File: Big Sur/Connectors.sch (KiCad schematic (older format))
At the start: 2 parts, among them J1 XT90, J2 XT90

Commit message: Work on pump drivers.
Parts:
- added J?: SMD CASTELLATION PKG, symbol Connector_Generic:Conn_02x21_Counter_Clockwise
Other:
- note added: "DON’T REALLY KNOW WHAT WE’RE DOING FOR CONNECTORS.\nSOMETHING ABOUT XT30/60/90S FOR POWER?"
- note added: "Strideduino"
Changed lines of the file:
@@
 Text Notes 1700 1600 0    118  ~ 0
 Power Input
+Text Notes 2950 2550 0    50   ~ 0
+DON’T REALLY KNOW WHAT WE’RE DOING FOR CONNECTORS.\nSOMETHING ABOUT XT30/60/90S FOR POWER?
+$Comp
+L Connector_Generic:Conn_02x21_Counter_Clockwise J?
+U 1 1 5D85E3A4
+P 2150 5350
+F 0 "J?" H 2200 6567 50  0000 C CNN
+F 1 "SMD CASTELLATION PKG" H 2200 6476 50  0000 C CNN
+F 2 "" H 2150 5350 50  0001 C CNN
+F 3 "~" H 2150 5350 50  0001 C CNN
+	1    2150 5350
+	1    0    0    -1
+$EndComp
+Text Notes 1700 4000 0    118  ~ 0
+Strideduino
 $EndSCHEMATC

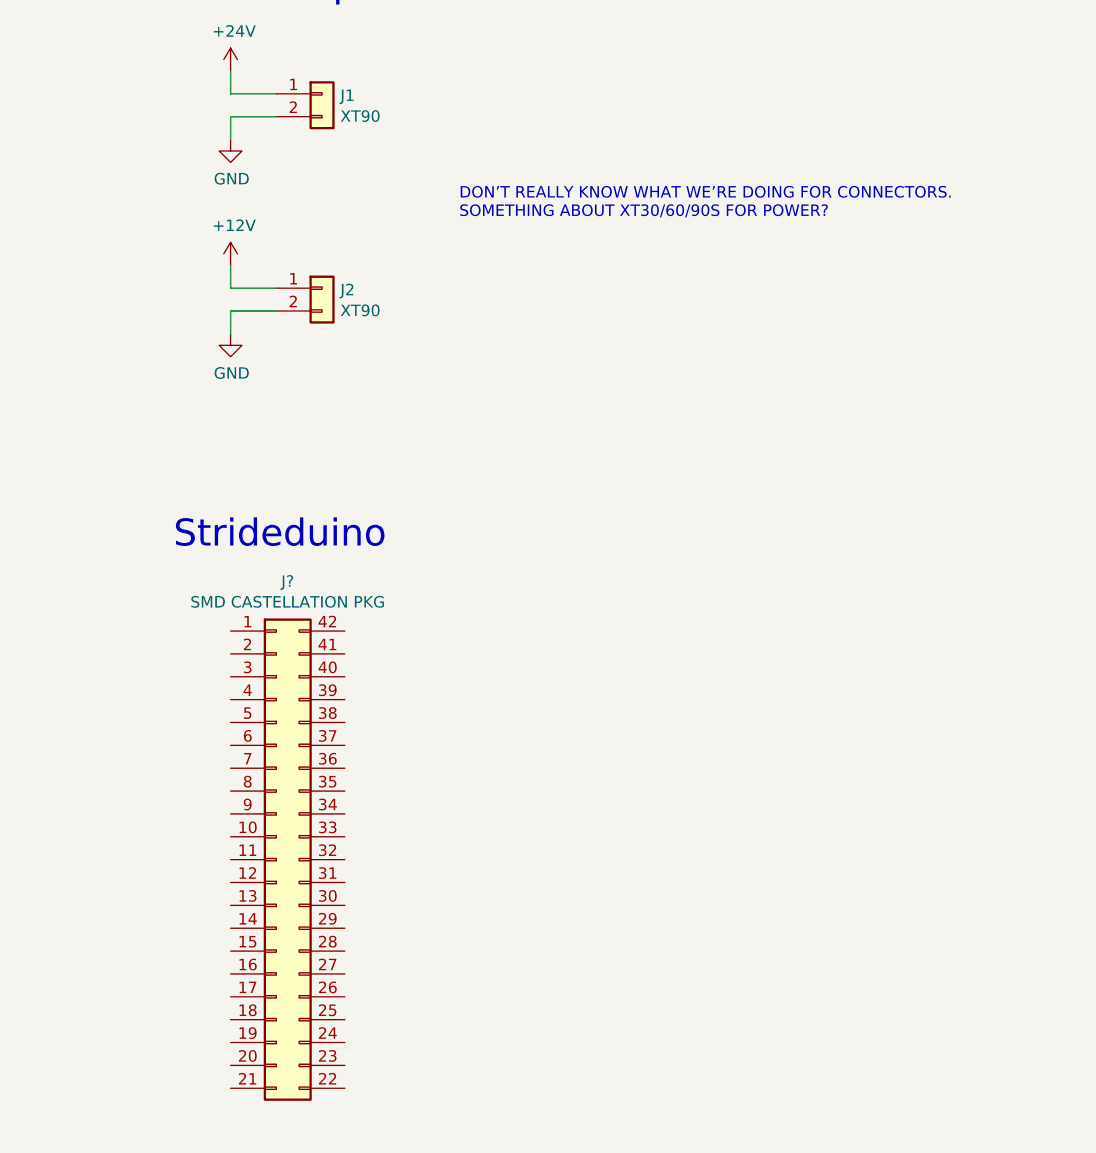
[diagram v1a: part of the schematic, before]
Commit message: Started filling in pinout of Paraduino connector, based on current Paraduino schematic.
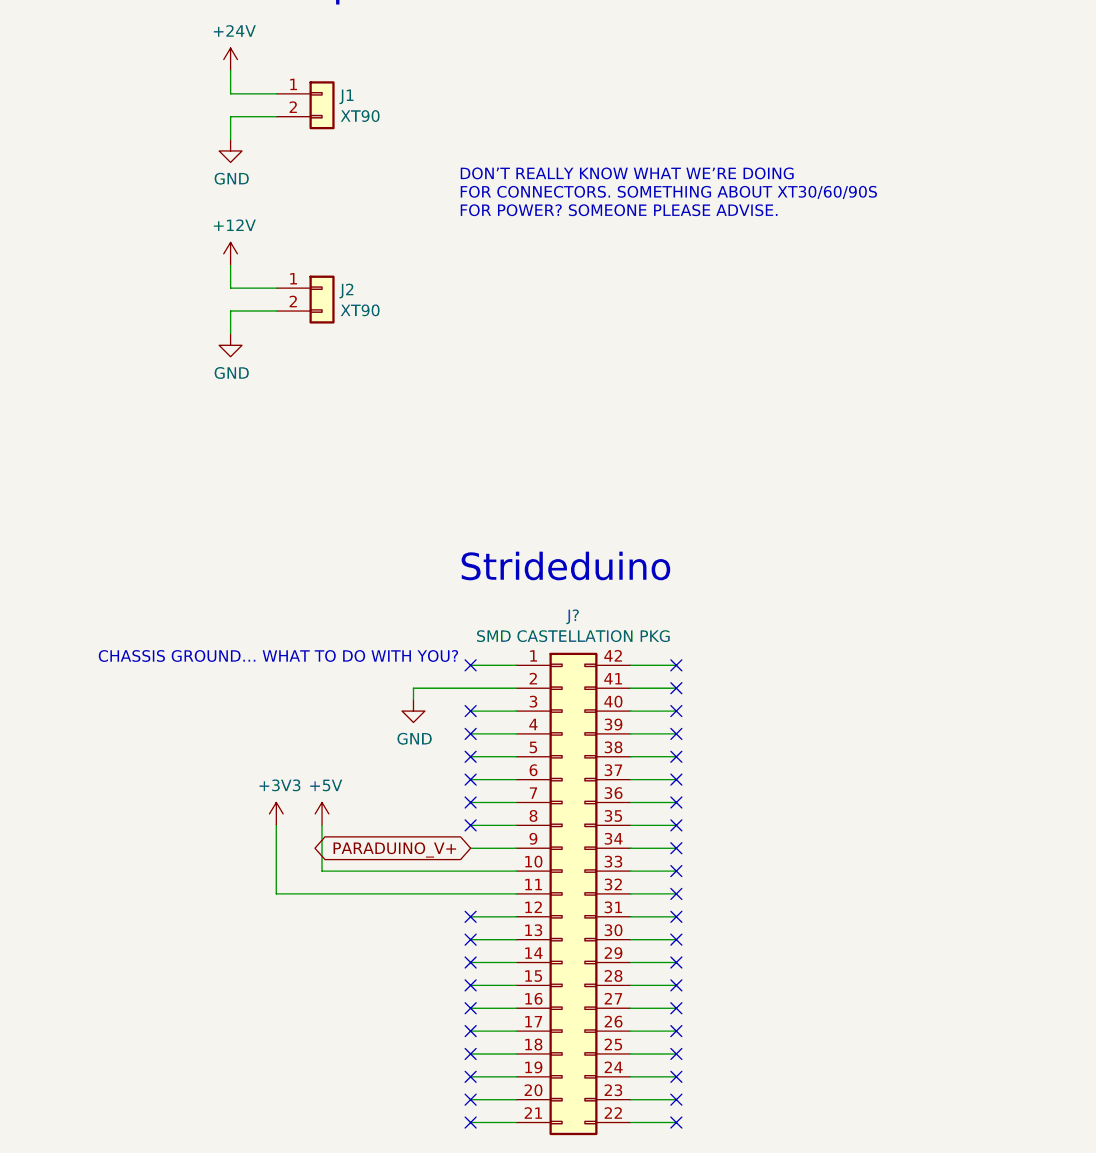
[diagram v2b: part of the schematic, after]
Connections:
- net GND: now also J?.2 (Pin_2)
- net +5V: now reaches J?.10 (Pin_10)
- net +3V3: now reaches J?.11 (Pin_11)
- net PARADUINO_V+: now reaches J?.9 (Pin_9)
- no-connect marks 0 -> 38
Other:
- note added: "CHASSIS GROUND… WHAT TO DO WITH YOU?"
- note added: "DON’T REALLY KNOW WHAT WE’RE DOING\nFOR CONNECTORS. SOMETHING ABOUT XT30/60/90S\nFOR POWER? SOMEONE PLEASE ADVISE."
- note removed: "DON’T REALLY KNOW WHAT WE’RE DOING FOR CONNECTORS.\nSOMETHING ABOUT XT30/60/90S FOR POWER?"
- moved on the sheet: J?
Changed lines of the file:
@@
 Power Input
 Text Notes 2950 2550 0    50   ~ 0
-DON’T REALLY KNOW WHAT WE’RE DOING FOR CONNECTORS.\nSOMETHING ABOUT XT30/60/90S FOR POWER?
+DON’T REALLY KNOW WHAT WE’RE DOING\nFOR CONNECTORS. SOMETHING ABOUT XT30/60/90S\nFOR POWER? SOMEONE PLEASE ADVISE.
 $Comp
 L Connector_Generic:Conn_02x21_Counter_Clockwise J?
 U 1 1 5D85E3A4
-P 2150 5350
-F 0 "J?" H 2200 6567 50  0000 C CNN
-F 1 "SMD CASTELLATION PKG" H 2200 6476 50  0000 C CNN
-F 2 "" H 2150 5350 50  0001 C CNN
-F 3 "~" H 2150 5350 50  0001 C CNN
-	1    2150 5350
+P 3400 5500
+F 0 "J?" H 3450 6717 50  0000 C CNN
+F 1 "SMD CASTELLATION PKG" H 3450 6626 50  0000 C CNN
+F 2 "" H 3400 5500 50  0001 C CNN
+F 3 "~" H 3400 5500 50  0001 C CNN
+	1    3400 5500
 	1    0    0    -1
 $EndComp
-Text Notes 1700 4000 0    118  ~ 0
+Text Notes 2950 4150 0    118  ~ 0
 Strideduino
+Wire Wire Line
+	3000 4500 3200 4500
+NoConn ~ 3000 4500
+Text Notes 2950 4500 2    50   ~ 0
+CHASSIS GROUND… WHAT TO DO WITH YOU?
+Wire Wire Line
+	3200 4600 2750 4600
+Wire Wire Line
+	2750 4600 2750 4650
+$Comp
+L power:GND #PWR?
+U 1 1 5D896FCF
+P 2750 4650
+F 0 "#PWR?" H 2750 4400 50  0001 C CNN
+F 1 "GND" H 2755 4477 50  0000 C CNN
+F 2 "" H 2750 4650 50  0001 C CNN
+F 3 "" H 2750 4650 50  0001 C CNN
+	1    2750 4650
+	1    0    0    -1
+$EndComp
+Wire Wire Line
+	3200 4700 3000 4700
+Wire Wire Line
+	3200 4800 3000 4800
+Wire Wire Line
+	3200 4900 3000 4900
+Wire Wire Line
+	3200 5000 3000 5000
+Wire Wire Line
+	3200 5100 3000 5100
+Wire Wire Line
+	3200 5200 3000 5200
+Wire Wire Line
+	3200 5600 3000 5600
+Wire Wire Line
+	3200 5700 3000 5700
+Wire Wire Line
+	3200 5800 3000 5800
+Wire Wire Line
+	3200 5900 3000 5900
+Wire Wire Line
+	3200 6000 3000 6000
+Wire Wire Line
+	3200 6100 3000 6100
+Wire Wire Line
+	3200 6200 3000 6200
+Wire Wire Line
+	3200 6300 3000 6300
+Wire Wire Line
+	3200 6400 3000 6400
+Wire Wire Line
+	3200 6500 3000 6500
+Wire Wire Line
+	3900 4700 3700 4700
+Wire Wire Line
+	3900 4800 3700 4800
+Wire Wire Line
+	3900 4900 3700 4900
+Wire Wire Line
+	3900 5000 3700 5000
+Wire Wire Line
+	3900 5100 3700 5100
+Wire Wire Line
+	3900 5200 3700 5200
+Wire Wire Line
+	3900 5300 3700 5300
+Wire Wire Line
+	3900 5400 3700 5400
+Wire Wire Line
+	3900 5500 3700 5500
+Wire Wire Line
+	3900 5600 3700 5600
+Wire Wire Line
+	3900 5700 3700 5700
+Wire Wire Line
+	3900 5800 3700 5800
+Wire Wire Line
+	3900 5900 3700 5900
+Wire Wire Line
+	3900 6000 3700 6000
+Wire Wire Line
+	3900 6100 3700 6100
+Wire Wire Line
+	3900 6200 3700 6200
+Wire Wire Line
+	3900 6300 3700 6300
+Wire Wire Line
+	3900 6400 3700 6400
+Wire Wire Line
+	3900 6500 3700 6500
+Wire Wire Line
+	3900 4500 3700 4500
+Wire Wire Line
+	3900 4600 3700 4600
+NoConn ~ 3900 4500
+NoConn ~ 3900 4600
+NoConn ~ 3900 4700
+NoConn ~ 3900 4800
+NoConn ~ 3900 4900
+NoConn ~ 3900 5000
+NoConn ~ 3900 5100
+NoConn ~ 3900 5200
+NoConn ~ 3900 5300
+NoConn ~ 3900 5400
+NoConn ~ 3900 5500
+NoConn ~ 3900 5600
+NoConn ~ 3900 5700
+NoConn ~ 3900 5800
+NoConn ~ 3900 5900
+NoConn ~ 3900 6000
+NoConn ~ 3900 6100
+NoConn ~ 3900 6200
+NoConn ~ 3900 6300
+NoConn ~ 3900 6400
+NoConn ~ 3900 6500
+NoConn ~ 3000 6500
+NoConn ~ 3000 6400
+NoConn ~ 3000 6300
+NoConn ~ 3000 6200
+NoConn ~ 3000 6100
+NoConn ~ 3000 6000
+NoConn ~ 3000 5900
+NoConn ~ 3000 5800
+NoConn ~ 3000 5700
+NoConn ~ 3000 5600
+NoConn ~ 3000 5200
+NoConn ~ 3000 5100
+NoConn ~ 3000 5000
+NoConn ~ 3000 4900
+NoConn ~ 3000 4800
+NoConn ~ 3000 4700
+$Comp
+L power:+5V #PWR?
+U 1 1 5D8BF1CA
+P 2350 5200
+F 0 "#PWR?" H 2350 5050 50  0001 C CNN
+F 1 "+5V" H 2365 5373 50  0000 C CNN
+F 2 "" H 2350 5200 50  0001 C CNN
+F 3 "" H 2350 5200 50  0001 C CNN
+	1    2350 5200
+	1    0    0    -1
+$EndComp
+Wire Wire Line
+	2350 5200 2350 5400
+Wire Wire Line
+	2350 5400 3200 5400
+$Comp
+L power:+3V3 #PWR?
+U 1 1 5D8C1FAE
+P 2150 5200
+F 0 "#PWR?" H 2150 5050 50  0001 C CNN
+F 1 "+3V3" H 2165 5373 50  0000 C CNN
+F 2 "" H 2150 5200 50  0001 C CNN
+F 3 "" H 2150 5200 50  0001 C CNN
+	1    2150 5200
+	1    0    0    -1
+$EndComp
+Wire Wire Line
+	2150 5200 2150 5500
+Wire Wire Line
+	2150 5500 3200 5500
+Wire Wire Line
+	3000 5300 3200 5300
+Text GLabel 3000 5300 0    50   BiDi ~ 0
+PARADUINO_V+
 $EndSCHEMATC

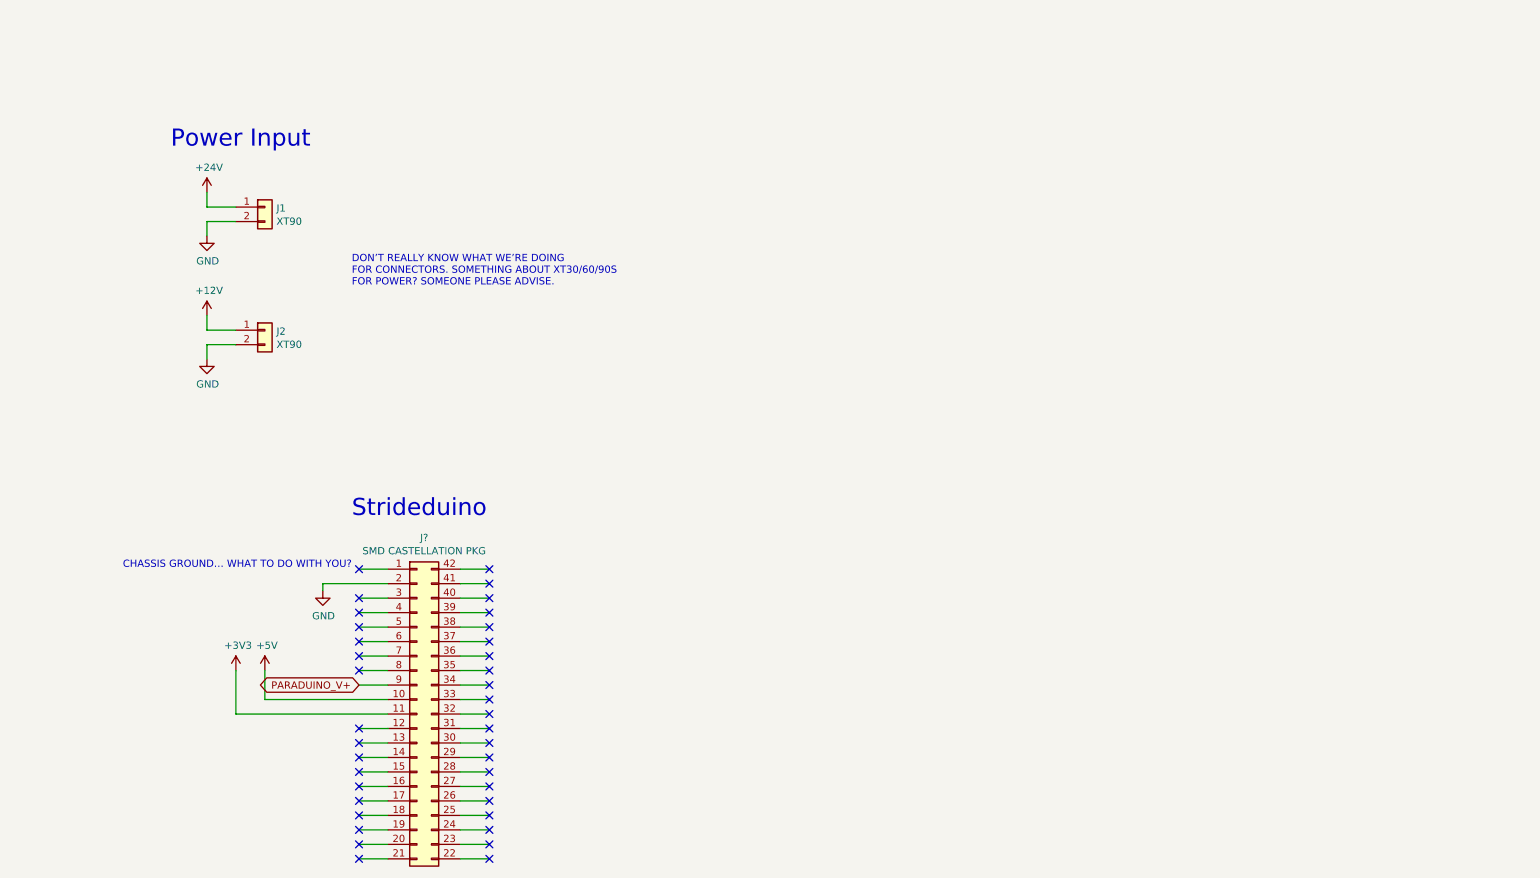
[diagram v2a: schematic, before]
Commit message: Updated current sense, second pump driver, solenoid connectors
-Current sense now uses current sense ICs, connected to Paraduino ADC pins.
-Added second pump driver.
-Connected outputs with XT30 connectors.
-Still need some Paraduino connections, inverter driver, footprints.
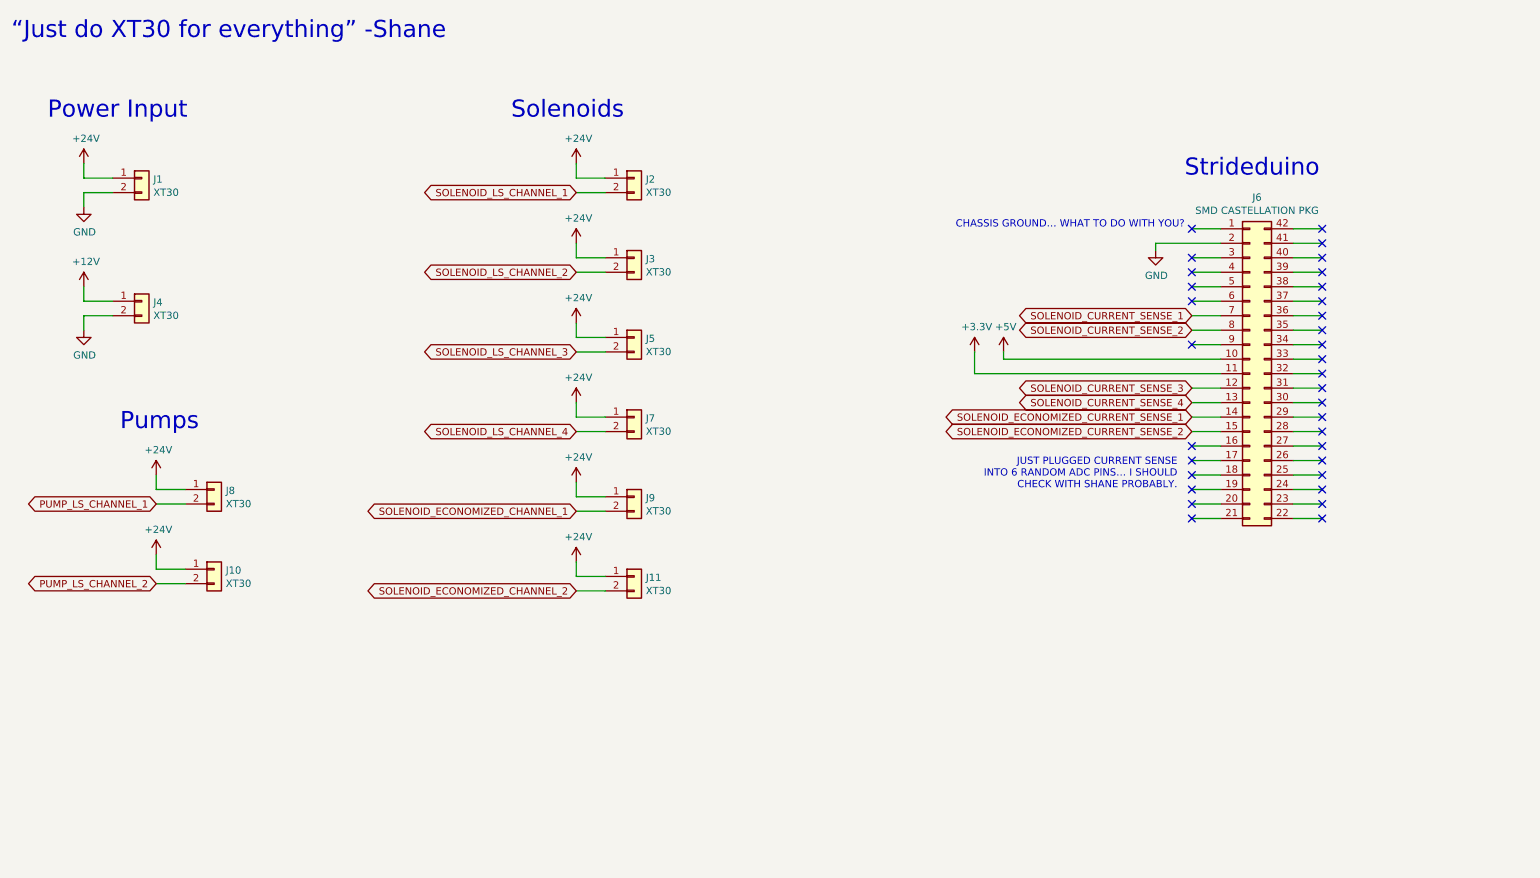
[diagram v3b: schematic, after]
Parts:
- added J10, J11, J2, J3, J5, J7, J8, J9: XT30, symbol Connector_Generic:Conn_01x02
- J1: value XT90 -> XT30
- J4: renamed from J2; value XT90 -> XT30
- gave numbers to parts that had none: 1
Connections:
- net +24V: now also J10.1 (Pin_1), J11.1 (Pin_1), J2.1 (Pin_1), J3.1 (Pin_1), J5.1 (Pin_1), J7.1 (Pin_1), J8.1 (Pin_1), J9.1 (Pin_1)
- net SOLENOID_CURRENT_SENSE_3: now reaches J6.12 (Pin_12)
- net SOLENOID_CURRENT_SENSE_4: now reaches J6.13 (Pin_13)
- net SOLENOID_ECONOMIZED_CURRENT_SENSE_1: now reaches J6.14 (Pin_14)
- net SOLENOID_ECONOMIZED_CURRENT_SENSE_2: now reaches J6.15 (Pin_15)
- net SOLENOID_CURRENT_SENSE_1: now reaches J6.7 (Pin_7)
- net SOLENOID_CURRENT_SENSE_2: now reaches J6.8 (Pin_8)
- net PARADUINO_V+: no longer names the net of J6.9 (Pin_9)
- new net PUMP_LS_CHANNEL_1: J8.2 (Pin_2)
- new net PUMP_LS_CHANNEL_2: J10.2 (Pin_2)
- new net SOLENOID_ECONOMIZED_CHANNEL_1: J9.2 (Pin_2)
- new net SOLENOID_ECONOMIZED_CHANNEL_2: J11.2 (Pin_2)
- new net SOLENOID_LS_CHANNEL_1: J2.2 (Pin_2)
- new net SOLENOID_LS_CHANNEL_2: J3.2 (Pin_2)
- new net SOLENOID_LS_CHANNEL_3: J5.2 (Pin_2)
- new net SOLENOID_LS_CHANNEL_4: J7.2 (Pin_2)
- no-connect marks 38 -> 33
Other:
- note added: "JUST PLUGGED CURRENT SENSE\nINTO 6 RANDOM ADC PINS… I SHOULD\nCHECK WITH SHANE PROBABLY."
- note added: "Pumps"
- note added: "Solenoids"
- note added: "“Just do XT30 for everything” -Shane"
- note removed: "DON’T REALLY KNOW WHAT WE’RE DOING\nFOR CONNECTORS. SOMETHING ABOUT XT30/60/90S\nFOR POWER? SOMEONE PLEASE ADVISE."
- moved on the sheet: J1, J4, J6

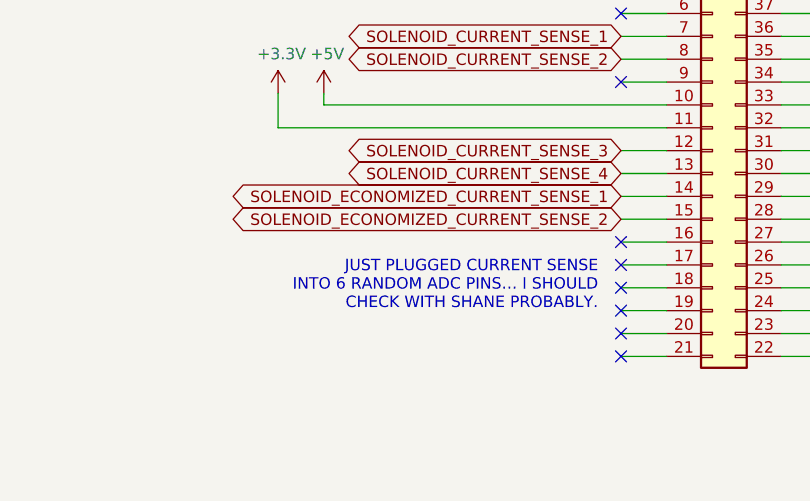
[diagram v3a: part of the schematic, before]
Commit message: Removed Inverter
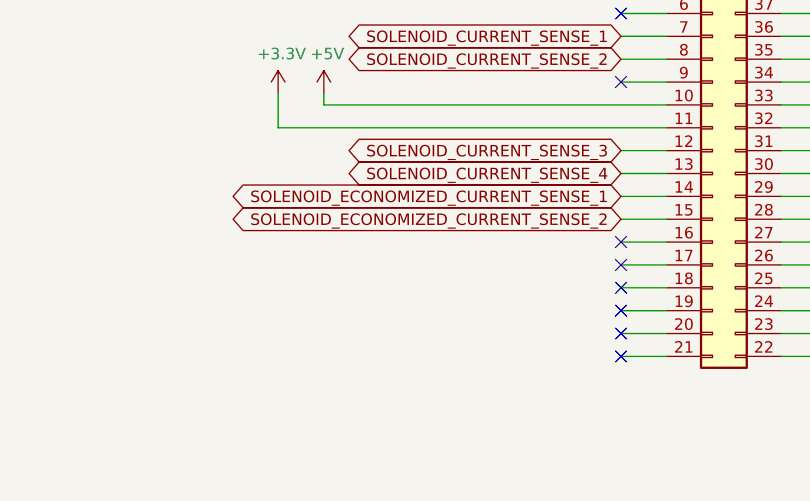
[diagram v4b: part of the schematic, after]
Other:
- note removed: "JUST PLUGGED CURRENT SENSE\nINTO 6 RANDOM ADC PINS… I SHOULD\nCHECK WITH SHANE PROBABLY."
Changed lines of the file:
@@
 Comp "Paradigm Hyperloop"
 Comment1 ""
-Comment2 ""
-Comment3 ""
+Comment2 "x"
+Comment3 "x"
 Comment4 "Jasper Rubin"
 $EndDescr
@@
 Text GLabel 8750 3550 0    50   BiDi ~ 0
 SOLENOID_ECONOMIZED_CURRENT_SENSE_2
-Text Notes 8650 3950 2    50   ~ 0
-JUST PLUGGED CURRENT SENSE\nINTO 6 RANDOM ADC PINS… I SHOULD\nCHECK WITH SHANE PROBABLY.
 $EndSCHEMATC
